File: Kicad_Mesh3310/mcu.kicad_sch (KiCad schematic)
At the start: 41 parts, among them J10 Conn_02x05_Odd_Even, U12 ZD25WQ16CTIGT, U13 NRF52840-QIAA-R, X2 S201632M10PF10PPM 32MHz, X4 32.768KHz

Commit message: Adding testpoints
Test pint on usb and SWD debug
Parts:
- removed J10: Conn_02x05_Odd_Even, Connector_PinHeader_1.27mm:PinHeader_2x05_P1.27mm_Vertical_SMD, symbol Connector_Generic:Conn_02x05_Odd_Even
- added TP13: RESET, TestPoint:TestPoint_Pad_D1.0mm, symbol Connector:TestPoint
- AE4, R55, TP6, TP7, TP8: now fitted
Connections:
- net RESETn: now also TP13.1
- no-connect marks 5 -> 4
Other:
- moved on the sheet: R49, R50, TP5

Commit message: Cleaning and placing
Cleaning and placing components
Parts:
- RF1: footprint lcsc:IPEX-SMD_3P-L2.6-W2.6-LS3.0_RF1200001R -> mesh3310_footprints:IPEX-SMD_3P-L2.6-W2.6-LS3.0_RF1200001R
- U12: footprint lcsc:SOIC-8_L4.9-W3.9-P1.27-LS6.0-BL -> mesh3310_footprints:SOIC-8_L4.9-W3.9-P1.27-LS6.0-BL
- U13: footprint mesh3310:XCVR_NRF52840-QIAA-R -> mesh3310_footprints:XCVR_NRF52840-QIAA-R
- X2: footprint mesh3310:CRYSTAL-SMD_4P-L2.0-W1.6-BL -> mesh3310_footprints:CRYSTAL-SMD_4P-L2.0-W1.6-BL
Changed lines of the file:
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@@
 			)
 		)
-		(property "Footprint" "lcsc:SOIC-8_L4.9-W3.9-P1.27-LS6.0-BL"
+		(property "Footprint" "mesh3310_footprints:SOIC-8_L4.9-W3.9-P1.27-LS6.0-BL"
 			(at 128.27 194.31 0)
 			(effects
@@
 			)
 		)
-		(property "Footprint" "lcsc:IPEX-SMD_3P-L2.6-W2.6-LS3.0_RF1200001R"
+		(property "Footprint" "mesh3310_footprints:IPEX-SMD_3P-L2.6-W2.6-LS3.0_RF1200001R"
 			(at 80.01 139.7 0)
 			(effects
@@
 			)
 		)
-		(property "Footprint" "mesh3310:CRYSTAL-SMD_4P-L2.0-W1.6-BL"
+		(property "Footprint" "mesh3310_footprints:CRYSTAL-SMD_4P-L2.0-W1.6-BL"
 			(at 30.48 27.94 0)
 			(effects
@@
 			)
 		)
-		(property "Footprint" "mesh3310:XCVR_NRF52840-QIAA-R"
+		(property "Footprint" "mesh3310_footprints:XCVR_NRF52840-QIAA-R"
 			(at 144.78 91.44 0)
 			(effects

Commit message: Start of routing
Component placing and start off routing
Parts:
- C36: footprint Capacitor_SMD:C_0603_1608Metric -> Capacitor_SMD:C_0402_1005Metric
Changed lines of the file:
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@@
 			)
 		)
-		(property "Footprint" "Capacitor_SMD:C_0603_1608Metric"
+		(property "Footprint" "Capacitor_SMD:C_0402_1005Metric"
 			(at 194.6148 71.12 0)
 			(effects

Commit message: RF designing
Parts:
- removed C33: .8pF, Capacitor_SMD:C_0402_1005Metric, symbol Device:C_Small
- removed NT1: NetTie_2, NetTie:NetTie-2_SMD_Pad0.5mm, symbol Device:NetTie_2
- removed R56: 0, Resistor_SMD:R_0402_1005Metric, symbol Device:R_Small
- removed RF1: A-IPEX1-1.25A, mesh3310_footprints:IPEX-SMD_3P-L2.6-W2.6-LS3.0_RF1200001R, symbol lcsc:A-IPEX1-1.25A
- added L1: 2.7nH, Inductor_SMD:L_0402_1005Metric, symbol Device:L
- AE4: footprint RF_Antenna:Texas_SWRA117D_2.4GHz_Right -> mesh3310_footprints:XCVR_2450AT18A0100001E; symbol Device:Antenna_Loop -> 2450AT18A0100001E:2450AT18A0100001E; Availability (none) -> In Stock; Check_prices (none) -> https://www.snapeda.com/parts/2450AT18A0100001E/Johanson/vi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; Description_1 (none) -> RF ANTENNA Chip Solder Surface Mount; MANUFACTURER (none) -> Johanson Technology; MAXIMUM_PACKAGE_HEIGHT (none) -> 1.40 mm; MF (none) -> Johanson Technology Inc.; MP (none) -> 2450AT18A0100001E; PARTREV (none) -> 4.0; Package (none) -> None; Price (none) -> None; Purchase-URL (none) -> https://www.snapeda.com/api/url_track_click_mouser/?unipart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; STANDARD (none) -> Manufacturer recommendations; SnapEDA_Link (none) -> https://www.snapeda.com/parts/2450AT18A0100001E/Johanson/vi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; now in the parts list
- C30: value .5pF -> 1.0pF
- L4: value 4.7nH -> 3.9nH
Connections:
- net ANT: now also C30.2
- net GND: no longer AE4.2, C30.2
- net VSS_PA: now also L1.1
- net at AE4.1, L4.1: no longer C30.1
- net at L4.2: now also C30.1, L1.2
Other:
- note removed: "Bluetooth antenna Implementing: https://www.lcsc.com/datasheet/C127620.pdf"
- moved on the sheet: C30

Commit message: cleanup
schematic cleanup
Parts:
- added C1: 100nF, Capacitor_SMD:C_0402_1005Metric, symbol Device:C_Small
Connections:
- net GND: now also C1.2
- net P0.06: now also C1.1
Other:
- moved on the sheet: AE4, C22, C29, C30, C31, C32, C34, C35, C36, C37, C38, C39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

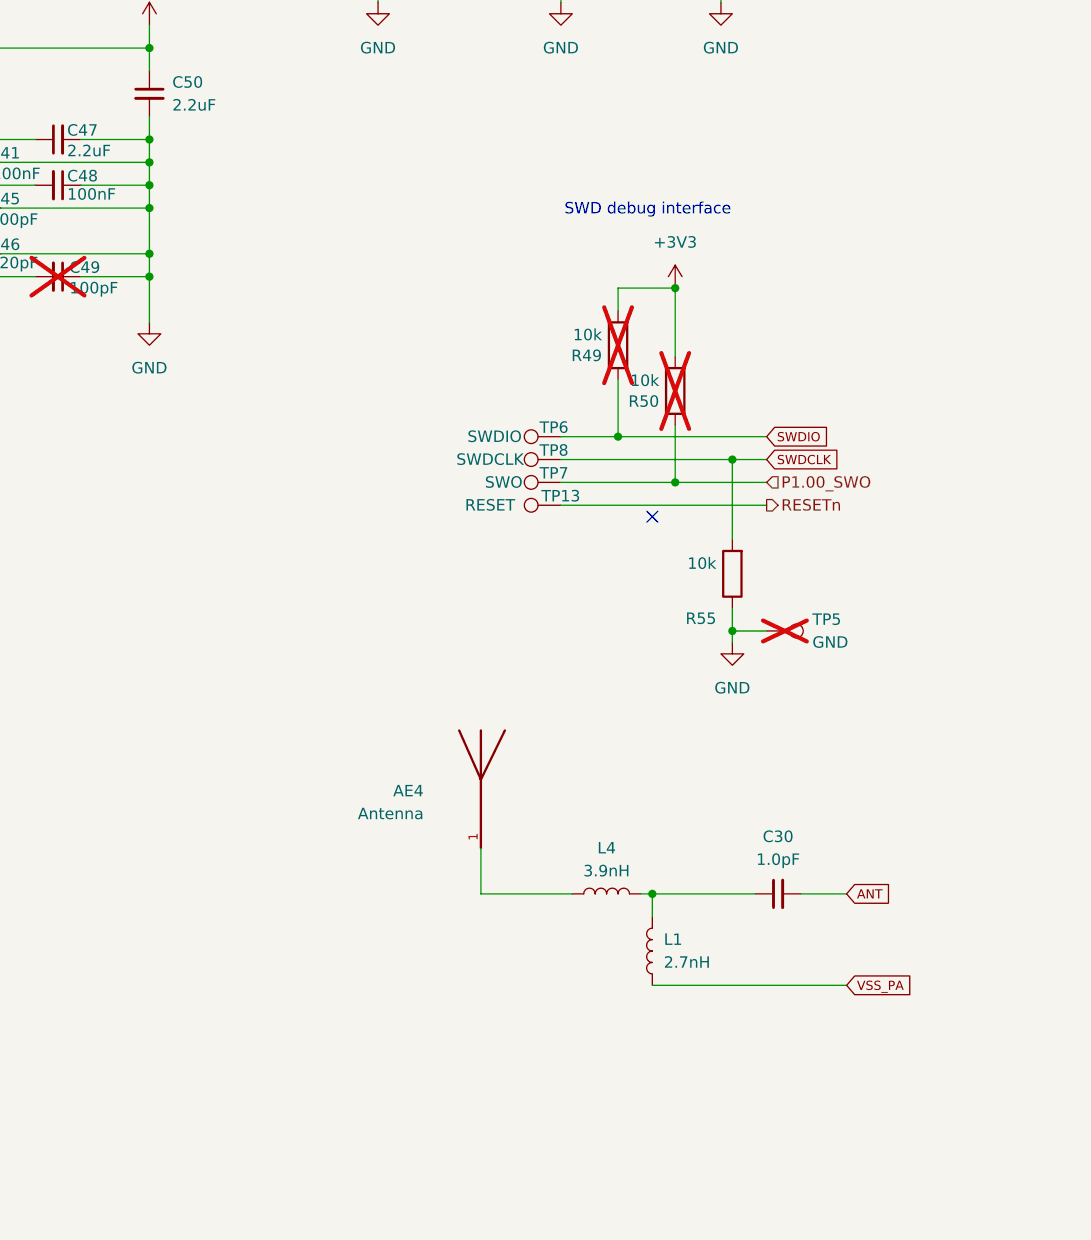
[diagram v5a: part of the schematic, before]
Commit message: Change antenna BT
BT change
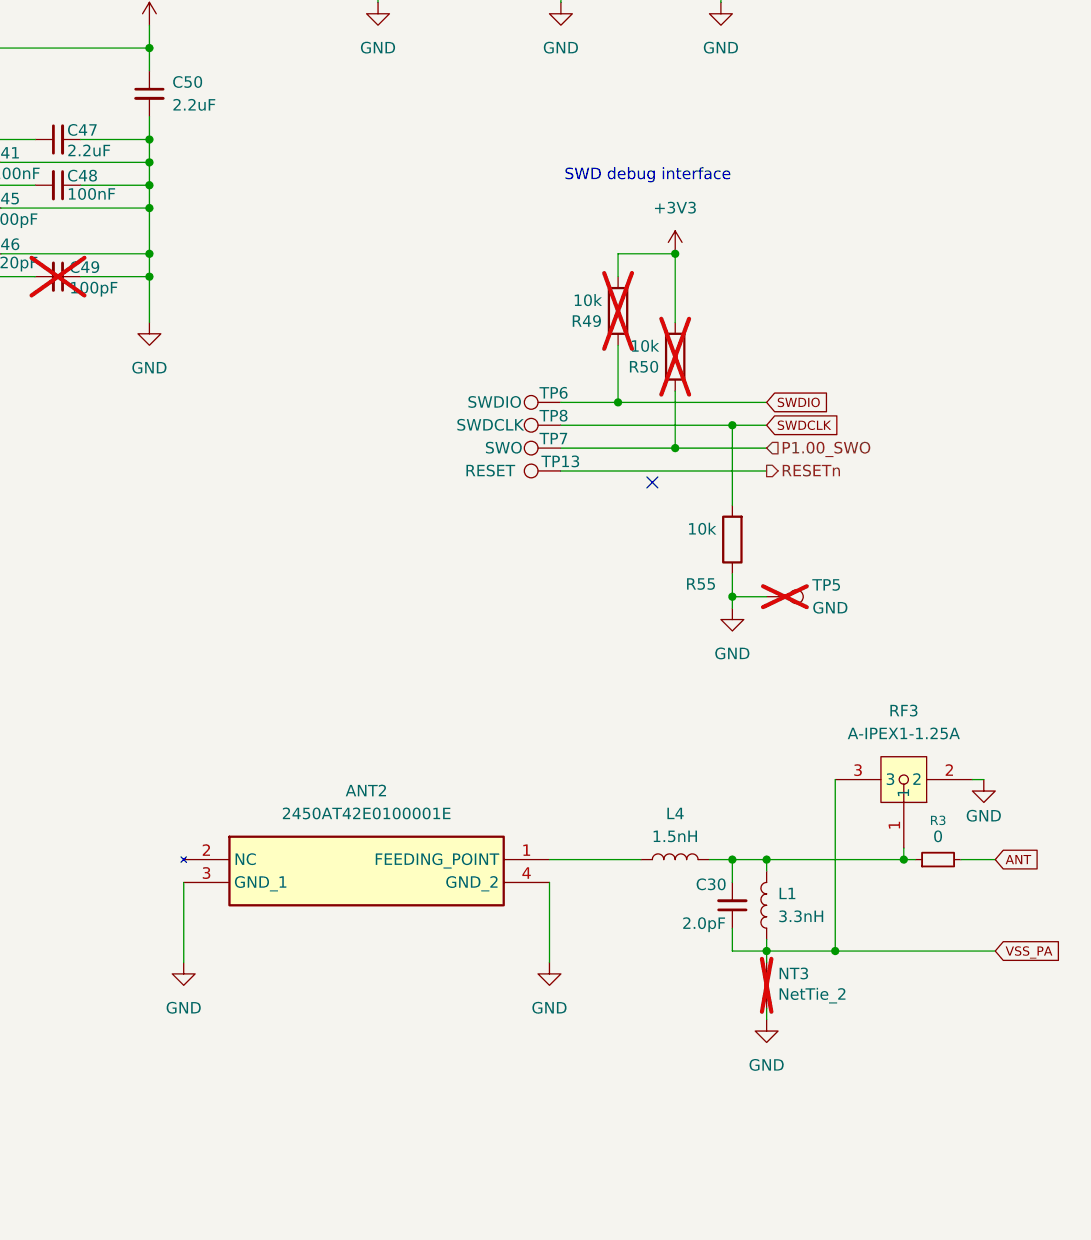
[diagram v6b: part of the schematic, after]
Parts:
- removed AE4: Antenna, mesh3310_footprints:XCVR_2450AT18A0100001E, symbol 2450AT18A0100001E:2450AT18A0100001E
- added ANT2: 2450AT42E0100001E, mesh3310_footprints:2450AT42E0100001E, symbol 2450AT42E0100001E:2450AT42E0100001E
- added NT3: NetTie_2, NetTie:NetTie-2_SMD_Pad0.5mm, symbol Device:NetTie_2
- added R3: 0, Resistor_SMD:R_0402_1005Metric, symbol Device:R_Small
- added RF3: A-IPEX1-1.25A, mesh3310_footprints:IPEX-SMD_3P-L2.6-W2.6-LS3.0_RF1200001R, symbol lcsc:A-IPEX1-1.25A
- C30: value 1.0pF -> 2.0pF
- L1: value 2.7nH -> 3.3nH
- L4: value 3.9nH -> 1.5nH
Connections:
- net ANT: now also R3.2; no longer C30.2
- net GND: now also ANT2.3 (GND_1), ANT2.4 (GND_2), NT3.1, RF3.2
- net VSS_PA: now also C30.1, NT3.2, RF3.3
- net at L4.1: now also ANT2.1 (FEEDING_POINT)
- net at L1.2, L4.2: now also C30.2, R3.1, RF3.1; no longer C30.1
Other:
- moved on the sheet: C30, L1, L4, R49, R50, R55, TP13, TP5, TP6, TP7, TP8

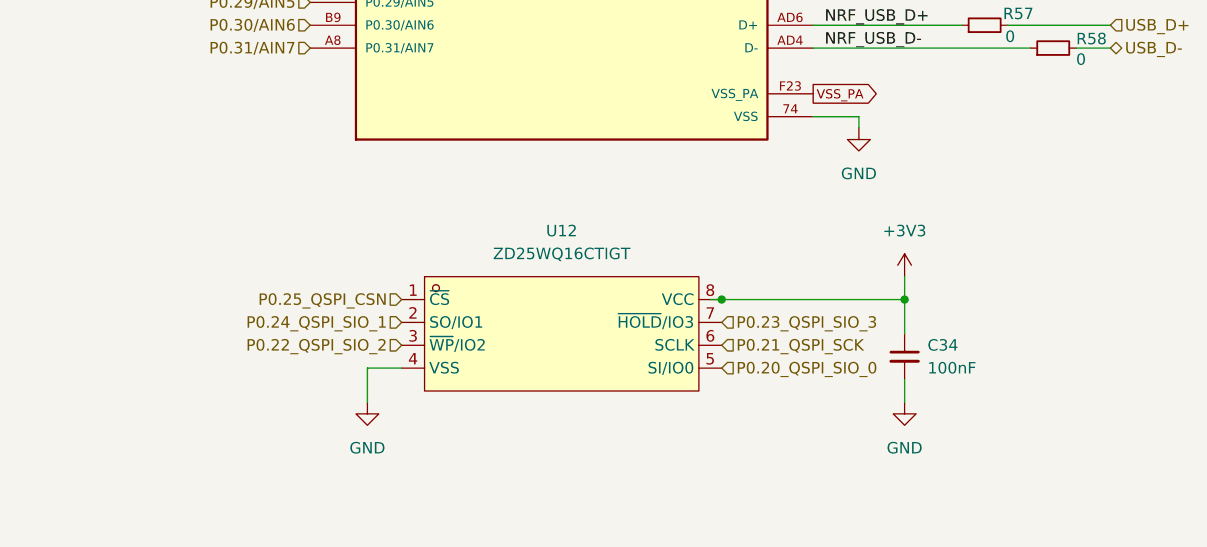
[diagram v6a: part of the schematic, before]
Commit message: Lora antenna replacement
Lora antenna replacement, added Nordic nRF 9151 for GPS , VoIP ,VoLTE-m , SIP
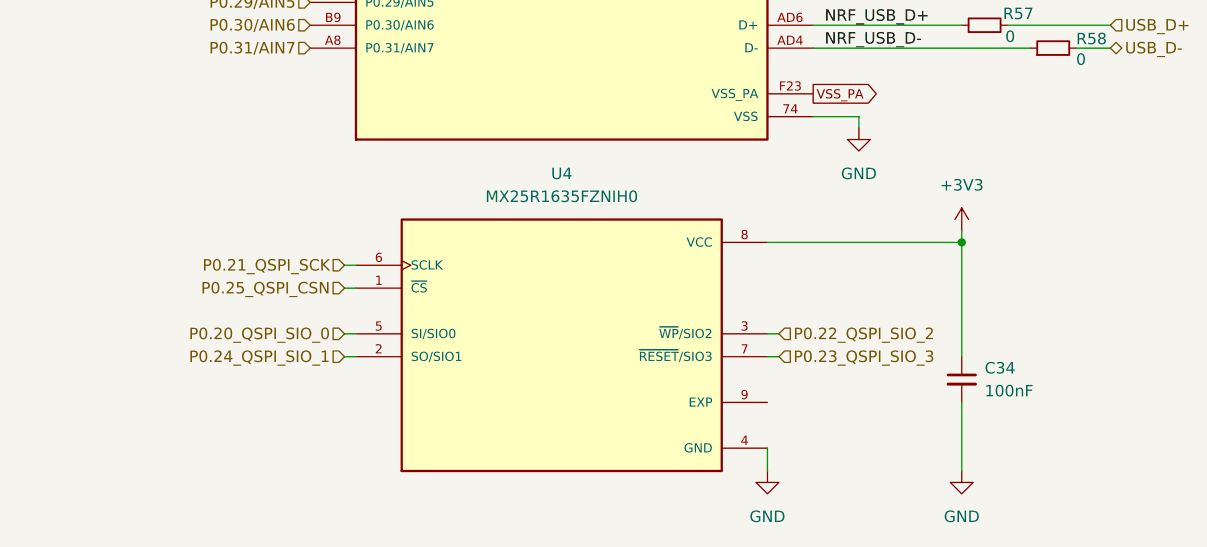
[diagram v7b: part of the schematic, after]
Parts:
- removed U12: ZD25WQ16CTIGT, mesh3310_footprints:SOIC-8_L4.9-W3.9-P1.27-LS6.0-BL, symbol lcsc:ZD25WQ16CTIGT
- added U4: MX25R1635FZNIH0, mesh3310_footprints:SON127P500X600X80-9N, symbol MX25R1635FZNIH0:MX25R1635FZNIH0
- C1, C22, C29, C30, C31, C32, C34, C35, C36, C37, C38, C39, C40, C41, C45, C46, C47, C48, C49, C50: footprint Capacitor_SMD:C_0402_1005Metric -> Capacitor_SMD:C_0201_0603Metric
- L1, L4, L6: footprint Inductor_SMD:L_0402_1005Metric -> Inductor_SMD:L_0201_0603Metric
- L5: footprint Inductor_SMD:L_0603_1608Metric -> Inductor_SMD:L_0201_0603Metric
- R3, R49, R50, R55, R57, R58: footprint Resistor_SMD:R_0402_1005Metric -> Resistor_SMD:R_0201_0603Metric
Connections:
- net +3V3: now also U4.8 (VCC)
- net GND: now also U4.4 (GND)
- net P0.20_QSPI_SIO_0: now also U4.5 (SI/SIO0)
- net P0.21_QSPI_SCK: now also U4.6 (SCLK)
- net P0.22_QSPI_SIO_2: now also U4.3 (~{WP}/SIO2)
- net P0.23_QSPI_SIO_3: now also U4.7 (~{RESET}/SIO3)
- net P0.24_QSPI_SIO_1: now also U4.2 (SO/SIO1)
- net P0.25_QSPI_CSN: now also U4.1 (~{CS})
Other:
- moved on the sheet: C34

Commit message: Backup work
Adding some extra pads
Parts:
- removed TP5: GND, TestPoint:TestPoint_Pad_D1.0mm, symbol Connector:TestPoint
- TP13, TP6, TP7, TP8: footprint TestPoint:TestPoint_Pad_D1.0mm -> TestPoint:TestPoint_Pad_D2.0mm
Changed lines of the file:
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@@
 	)
 	(junction
-		(at 242.57 110.49)
-		(diameter 0)
-		(color 0 0 0 0)
-	)
-	(junction
 		(at 134.62 69.85)
 		(diameter 0)
@@
 	(wire
 		(pts
-			(xy 246.38 110.49) (xy 242.57 110.49)
-		)
-		(stroke
-			(width 0)
-			(type default)
-		)
-	)
-	(wire
-		(pts
 			(xy 242.57 91.44) (xy 246.38 91.44)
 		)
@@
 	(wire
 		(pts
-			(xy 242.57 107.95) (xy 242.57 110.49)
+			(xy 242.57 107.95) (xy 242.57 111.76)
 		)
 		(stroke
@@
 	(wire
 		(pts
-			(xy 242.57 111.76) (xy 242.57 110.49)
-		)
-		(stroke
-			(width 0)
-			(type default)
-		)
-	)
-	(wire
-		(pts
 			(xy 210.82 26.67) (xy 215.9 26.67)
 		)
@@
 			)
 		)
-		(property "Footprint" "TestPoint:TestPoint_Pad_D1.0mm"
+		(property "Footprint" "TestPoint:TestPoint_Pad_D2.0mm"
 			(at 223.52 88.9 0)
 			(effects
@@
 	)
 	(symbol
-		(lib_id "Connector:TestPoint")
-		(at 246.38 110.49 270)
-		(unit 1)
-		(exclude_from_sim no)
-		(in_bom no)
-		(on_board yes)
-		(dnp yes)
-		(fields_autoplaced yes)
-		(property "Reference" "TP5"
-			(at 251.46 109.2199 90)
-			(effects
-				(font
-					(size 1.27 1.27)
-				)
-				(justify left)
-			)
-		)
-		(property "Value" "GND"
-			(at 251.46 111.7599 90)
-			(effects
-				(font
-					(size 1.27 1.27)
-				)
-				(justify left)
-			)
-		)
-		(property "Footprint" "TestPoint:TestPoint_Pad_D1.0mm"
-			(at 246.38 115.57 0)
-			(effects
-				(font
-					(size 1.27 1.27)
-				)
-				(hide yes)
-			)
-		)
-		(property "Datasheet" "~"
-			(at 246.38 115.57 0)
-			(effects
-				(font
-					(size 1.27 1.27)
-				)
-				(hide yes)
-			)
-		)
-		(property "Description" "test point"
-			(at 246.38 110.49 0)
-			(effects
-				(font
-					(size 1.27 1.27)
-				)
-				(hide yes)
-			)
-		)
-		(property "pin1" ""
-			(at 246.38 110.49 0)
-			(effects
-				(font
-					(size 1.27 1.27)
-				)
-				(hide yes)
-			)
-		)
-		(property "pin2" ""
-			(at 246.38 110.49 0)
-			(effects
-				(font
-					(size 1.27 1.27)
-				)
-				(hide yes)
-			)
-		)
-		(property "pin3" ""
-			(at 246.38 110.49 0)
-			(effects
-				(font
-					(size 1.27 1.27)
-				)
-				(hide yes)
-			)
-		)
-		(property "pin4" ""
-			(at 246.38 110.49 0)
-			(effects
-				(font
-					(size 1.27 1.27)
-				)
-				(hide yes)
-			)
-		)
-		(property "pin5" ""
-			(at 246.38 110.49 0)
-			(effects
-				(font
-					(size 1.27 1.27)
-				)
-				(hide yes)
-			)
-		)
-		(pin "1"
-		)
-		(instances
-			(project "Mesh3310"
-				(path "/8d65c5ef-7a02-4454-aee5-ab9c49e4aeab/62adca03-0f5f-4aef-8e1e-363483f74622"
-					(reference "TP5")
-					(unit 1)
-				)
-			)
-		)
-	)
-	(symbol
 		(lib_id "power:GND")
 		(at 96.52 190.5 0)
@@
 			)
 		)
-		(property "Footprint" "TestPoint:TestPoint_Pad_D1.0mm"
+		(property "Footprint" "TestPoint:TestPoint_Pad_D2.0mm"
 			(at 223.52 91.44 0)
 			(effects
@@
 			)
 		)
-		(property "Footprint" "TestPoint:TestPoint_Pad_D1.0mm"
+		(property "Footprint" "TestPoint:TestPoint_Pad_D2.0mm"
 			(at 223.52 83.82 0)
 			(effects
@@
 			)
 		)
-		(property "Footprint" "TestPoint:TestPoint_Pad_D1.0mm"
+		(property "Footprint" "TestPoint:TestPoint_Pad_D2.0mm"
 			(at 223.52 86.36 0)
 			(effects
